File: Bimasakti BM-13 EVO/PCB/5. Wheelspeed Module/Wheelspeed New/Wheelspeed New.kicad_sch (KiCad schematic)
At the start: 21 parts, among them J3 Conn_01x15_Pin, J4 Conn_01x15_Pin, U1 ESP32-C3_SUPERMINI_TH, U2 LM393

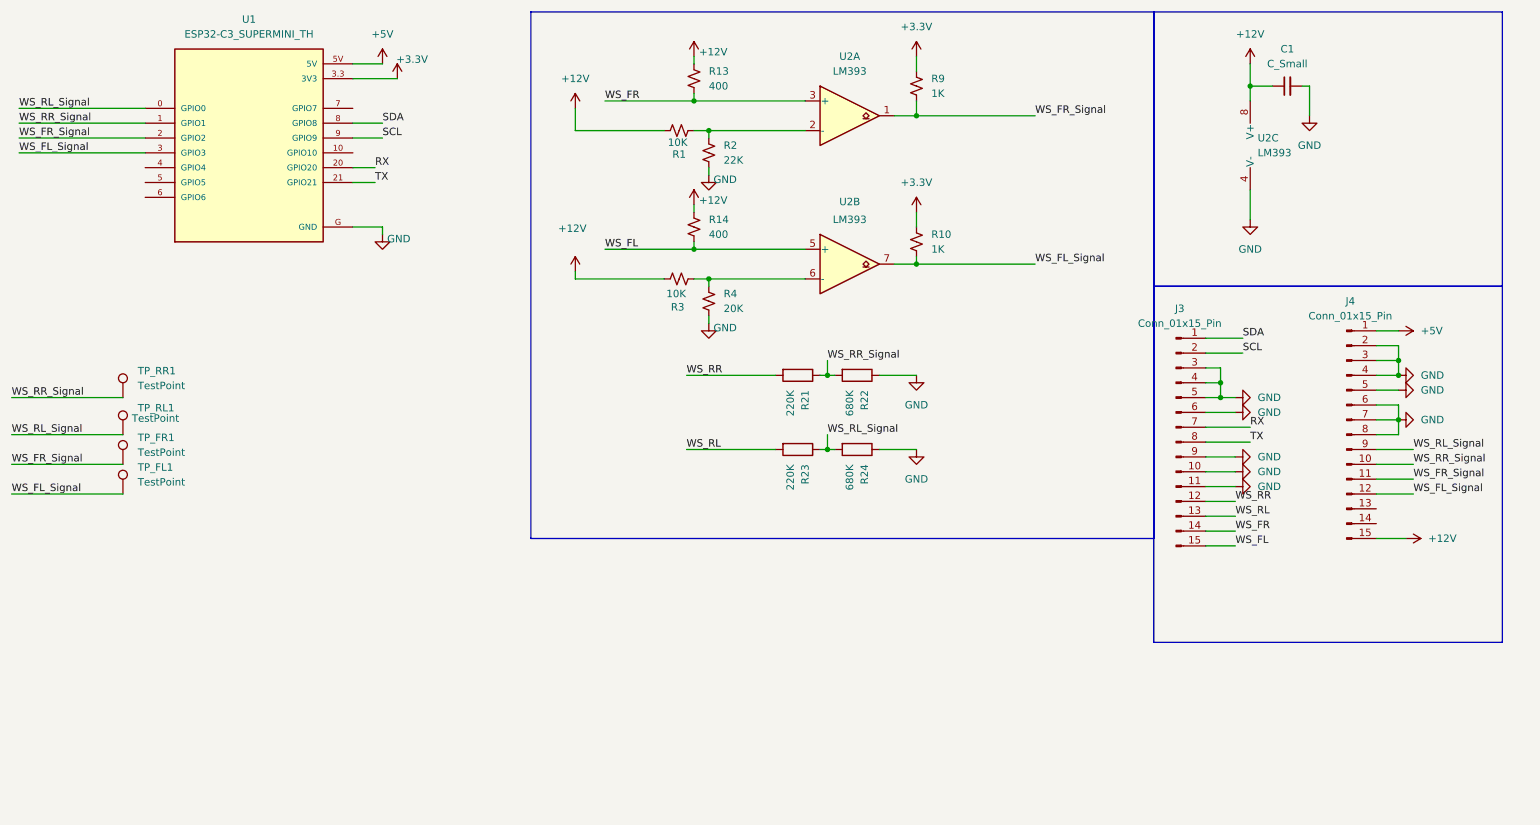
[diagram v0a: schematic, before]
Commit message: tambah level shifter karena mau dibuat traction control
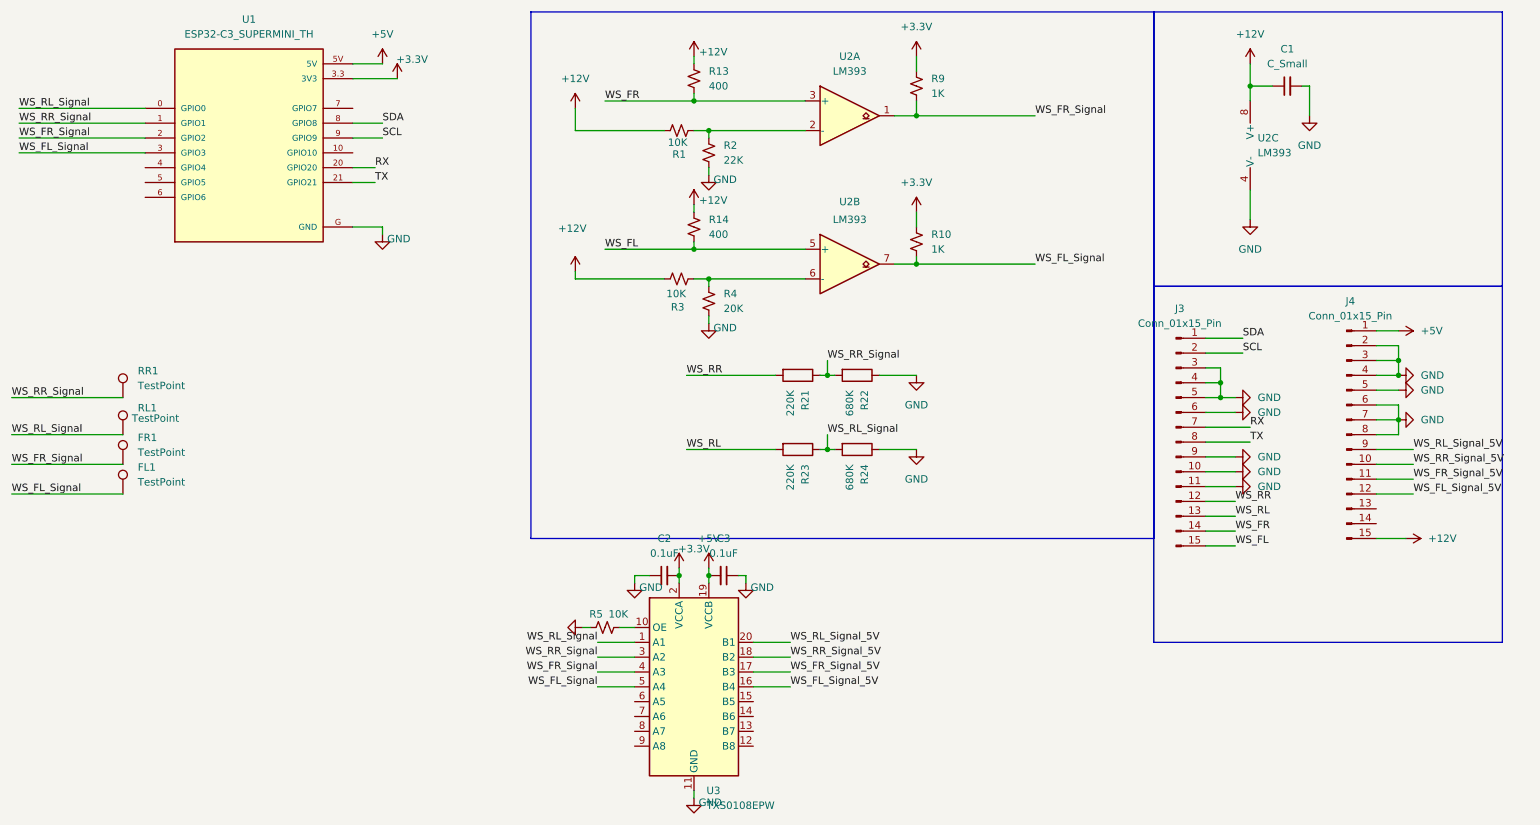
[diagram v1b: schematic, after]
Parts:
- added C2, C3: 0.1uF, Capacitor_SMD:C_0603_1608Metric_Pad1.08x0.95mm_HandSolder, symbol Device:C_Small
- added R5: 10K, Resistor_SMD:R_0603_1608Metric_Pad0.98x0.95mm_HandSolder, symbol Device:R_Small_US
- added U3: TXS0108EPW, Package_SO:TSSOP-20_4.4x6.5mm_P0.65mm, symbol Logic_LevelTranslator:TXS0108EPW
- renumbered TP_FL1 to FL1, TP_FR1 to FR1, TP_RL1 to RL1, TP_RR1 to RR1
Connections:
- net +3.3V: now also C2.2, U3.2 (VCCA)
- net +5V: now also C3.2, U3.19 (VCCB)
- net GND: now also C2.1, C3.1, R5.1, U3.11 (GND)
- net WS_FL_Signal: now also U3.5 (A4); no longer J4.12 (Pin_12)
- net WS_FR_Signal: now also U3.4 (A3); no longer J4.11 (Pin_11)
- net WS_RL_Signal: now also U3.1 (A1); no longer J4.9 (Pin_9)
- net WS_RR_Signal: now also U3.3 (A2); no longer J4.10 (Pin_10)
- new net: R5.2, U3.10 (OE)
- new net WS_FL_Signal_5V: J4.12 (Pin_12), U3.16 (B4)
- new net WS_FR_Signal_5V: J4.11 (Pin_11), U3.17 (B3)
- new net WS_RL_Signal_5V: J4.9 (Pin_9), U3.20 (B1)
- new net WS_RR_Signal_5V: J4.10 (Pin_10), U3.18 (B2)
